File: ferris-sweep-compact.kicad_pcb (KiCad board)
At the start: 2 copper layers, 109.2 x 87.5 mm, 22 parts, among them J1 MJ-4PP-9, SW10 SW_PUSH, SW11 SW_PUSH, SW12 SW_PUSH, SW14 SW_PUSH, SW15 SW_PUSH, SW16 SW_PUSH, SW17 SW_PUSH, SW18 SW_PUSH, SW2 SW_PUSH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

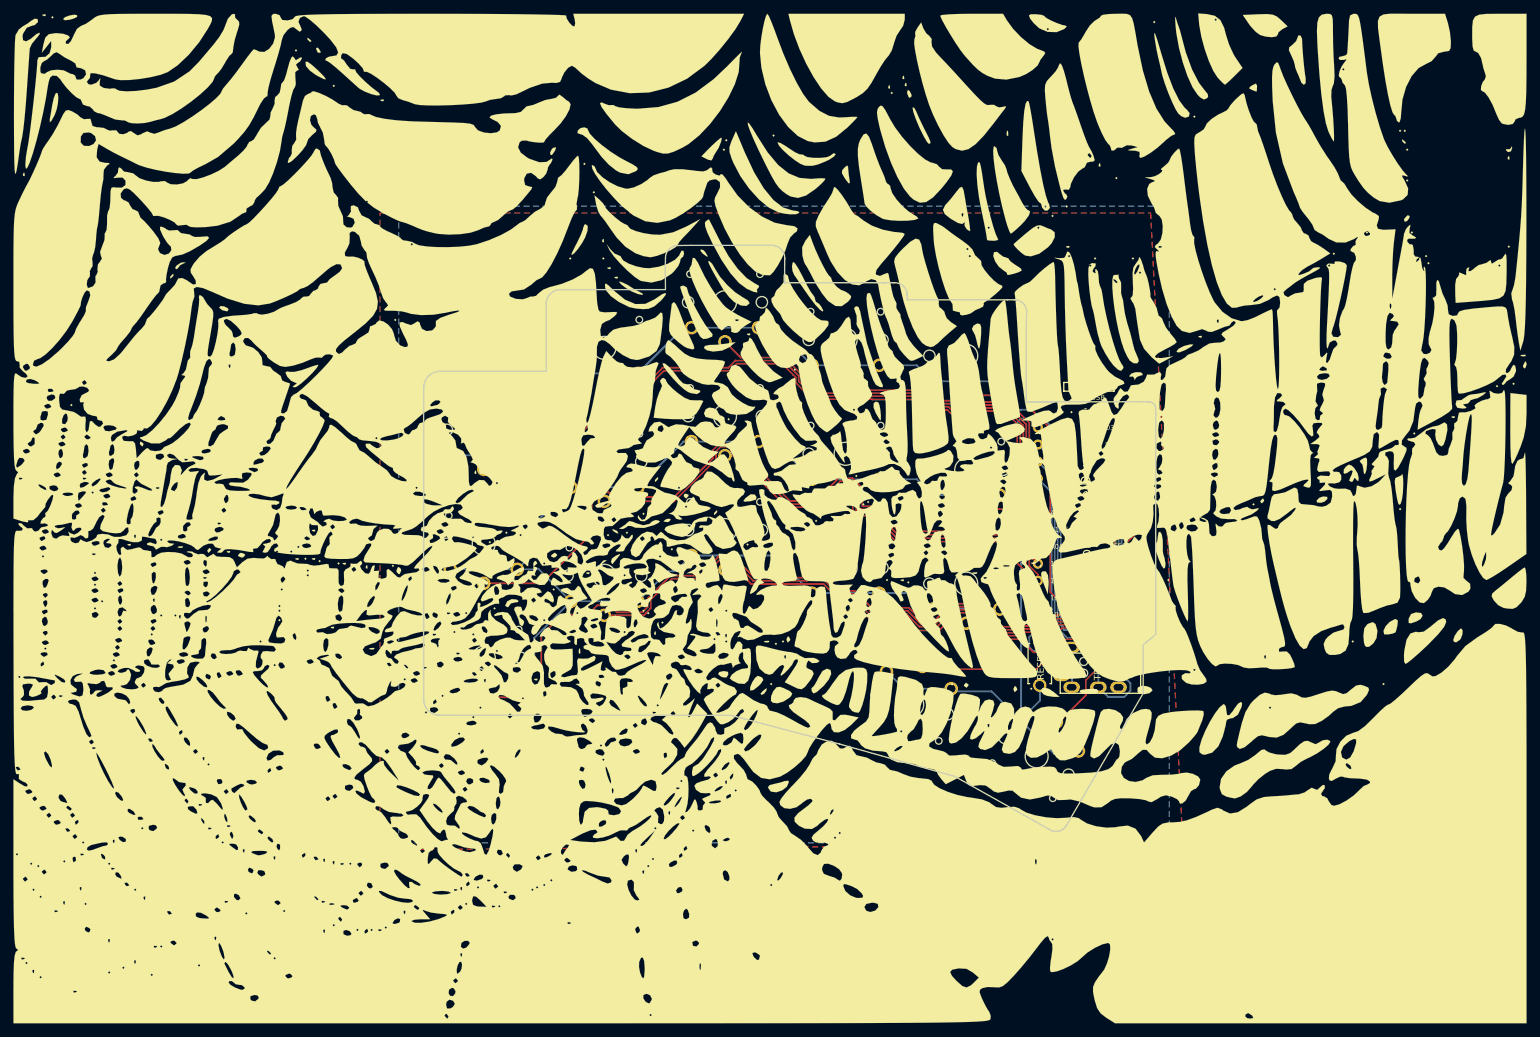
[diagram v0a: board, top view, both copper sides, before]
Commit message: Updated edge cuts
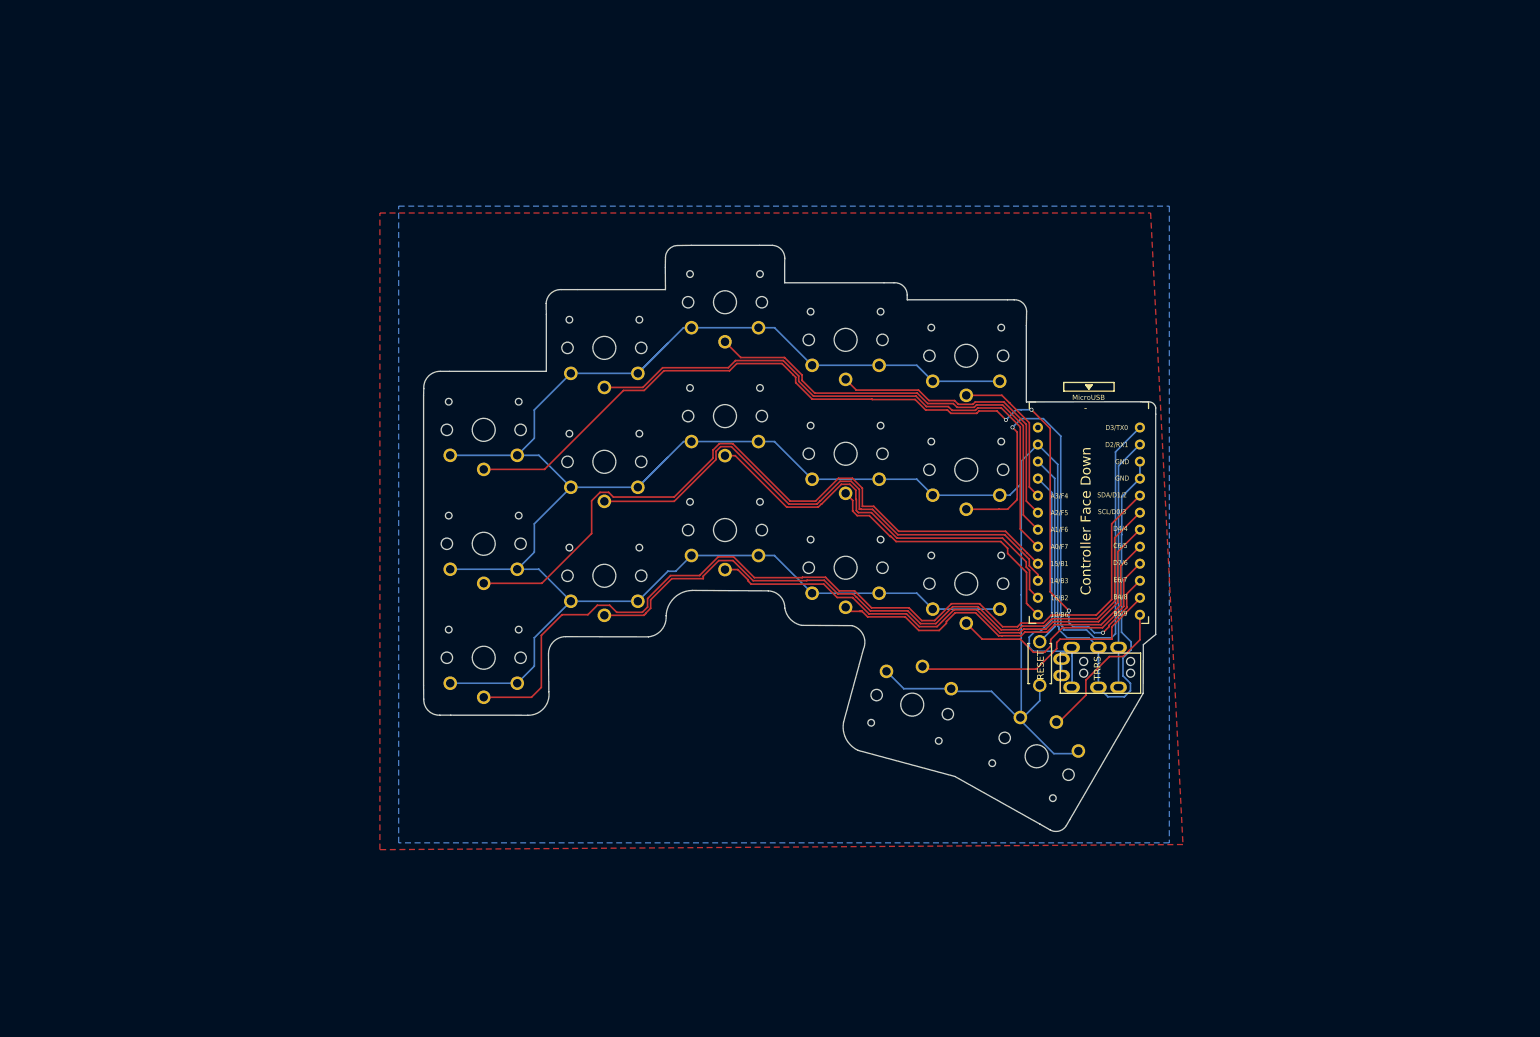
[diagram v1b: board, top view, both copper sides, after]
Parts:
- removed G*** (x2): LOGO, Desktop:web
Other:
- outline, holes or cut-outs redrawn
- net class Default removed

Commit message: Added text layer and finished edge cuts
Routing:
- net GND: track 490.3 -> 477.4 mm
- net VCC: track 41.9 -> 40.7 mm
- net row1: track 57.5 -> 57.0 mm
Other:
- board text added: "Appman & son"
